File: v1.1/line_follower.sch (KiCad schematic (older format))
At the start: 25 parts, among them K1 BUZZER, P1 QTR-8A, P2 HC-05, P3 EXP HEADER, P4 LEFT MOTOR, P5 RIGHT MOTOR, P6 BATTERY, SW1 SW_PUSH, SW2 SW_PUSH, SW3 SW_PUSH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

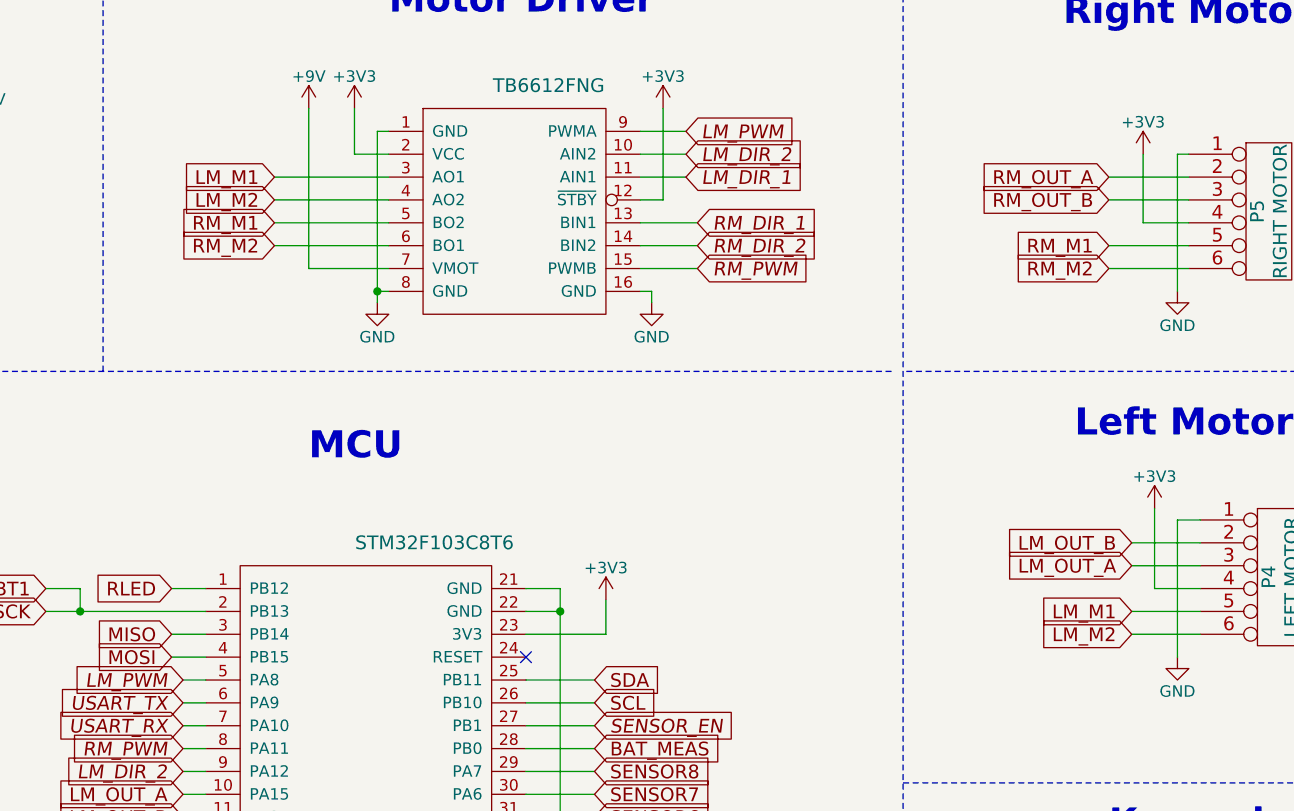
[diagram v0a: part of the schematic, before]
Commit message: Small cosmetic changes. Include schematic in PNG format.
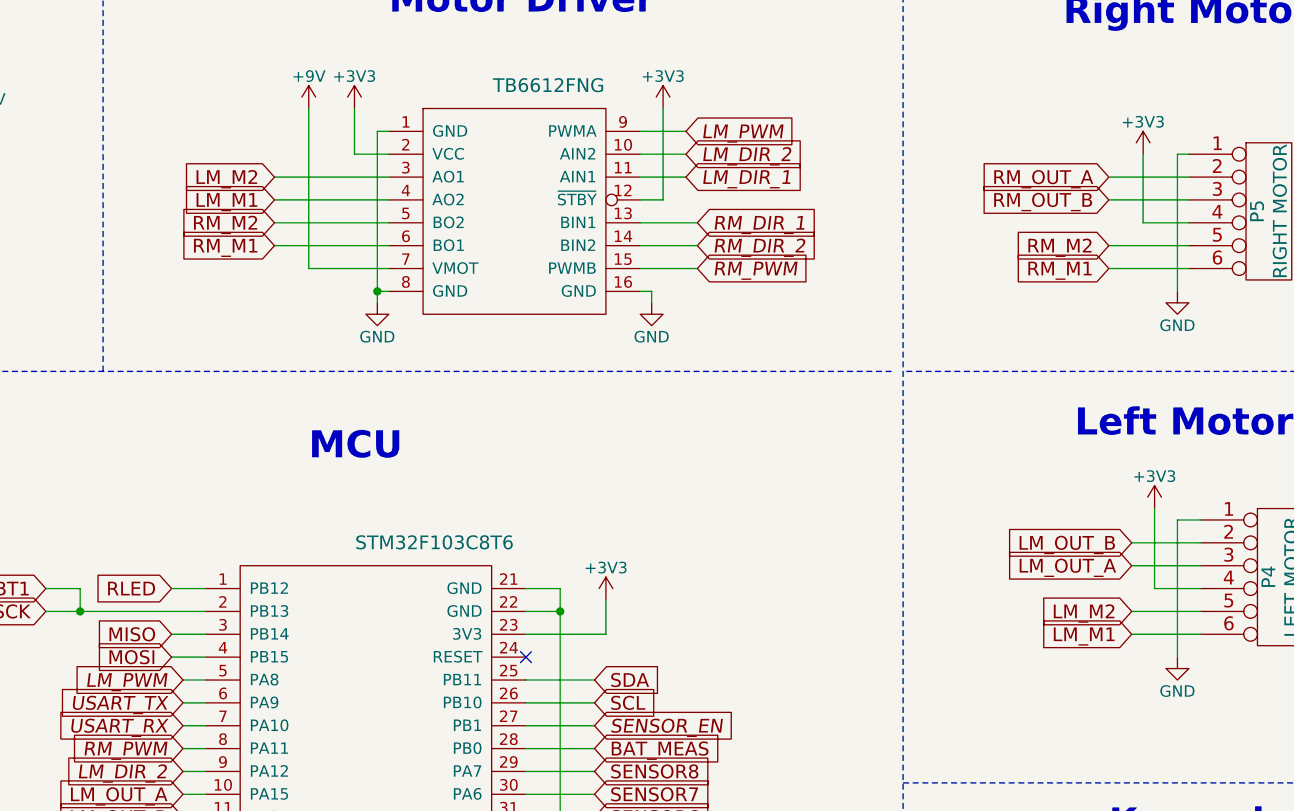
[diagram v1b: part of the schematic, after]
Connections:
- net LM_M1: now also P4.6, U7.4 (AO2); no longer P4.5, U7.3 (AO1)
- net LM_M2: now also P4.5, U7.3 (AO1); no longer P4.6, U7.4 (AO2)
- net RM_M1: now also P5.6, U7.6 (BO1); no longer P5.5, U7.5 (BO2)
- net RM_M2: now also P5.5, U7.5 (BO2); no longer P5.6, U7.6 (BO1)
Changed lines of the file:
@@
 EESchema Schematic File Version 4
 LIBS:line_follower-cache
-EELAYER 26 0
+EELAYER 29 0
 EELAYER END
 $Descr A4 11693 8268
@@
 RM_OUT_B
 Text GLabel 9750 1800 0    60   Input ~ 0
+RM_M2
+Text GLabel 9750 1900 0    60   Input ~ 0
 RM_M1
-Text GLabel 9750 1900 0    60   Input ~ 0
+Text GLabel 6100 1700 0    60   Input ~ 0
 RM_M2
-Text GLabel 6100 1700 0    60   Input ~ 0
+Text GLabel 6100 1800 0    60   Input ~ 0
 RM_M1
-Text GLabel 6100 1800 0    60   Input ~ 0
-RM_M2
 Text GLabel 6100 1600 0    60   Input ~ 0
+LM_M1
+Text GLabel 6100 1500 0    60   Input ~ 0
 LM_M2
-Text GLabel 6100 1500 0    60   Input ~ 0
+Text GLabel 9850 3400 0    60   Input ~ 0
+LM_M2
+Text GLabel 9850 3500 0    60   Input ~ 0
 LM_M1
-Text GLabel 9850 3400 0    60   Input ~ 0
-LM_M1
-Text GLabel 9850 3500 0    60   Input ~ 0
-LM_M2
 Text GLabel 9850 3200 0    60   Input ~ 0
 LM_OUT_A
